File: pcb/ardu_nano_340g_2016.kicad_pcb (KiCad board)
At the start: 2 copper layers, 18.3 x 43.7 mm, 36 parts, among them J1 USB_B_Mini, J2 Conn_01x15, J3 Conn_01x15, J4 Conn_02x03_Odd_Even, U1 CH340G-JEC, U2 ATMEGA328P-AU, U3 LM1117-5.0, Y1 16MHz Resonator, Y2 12Mhz Resonator

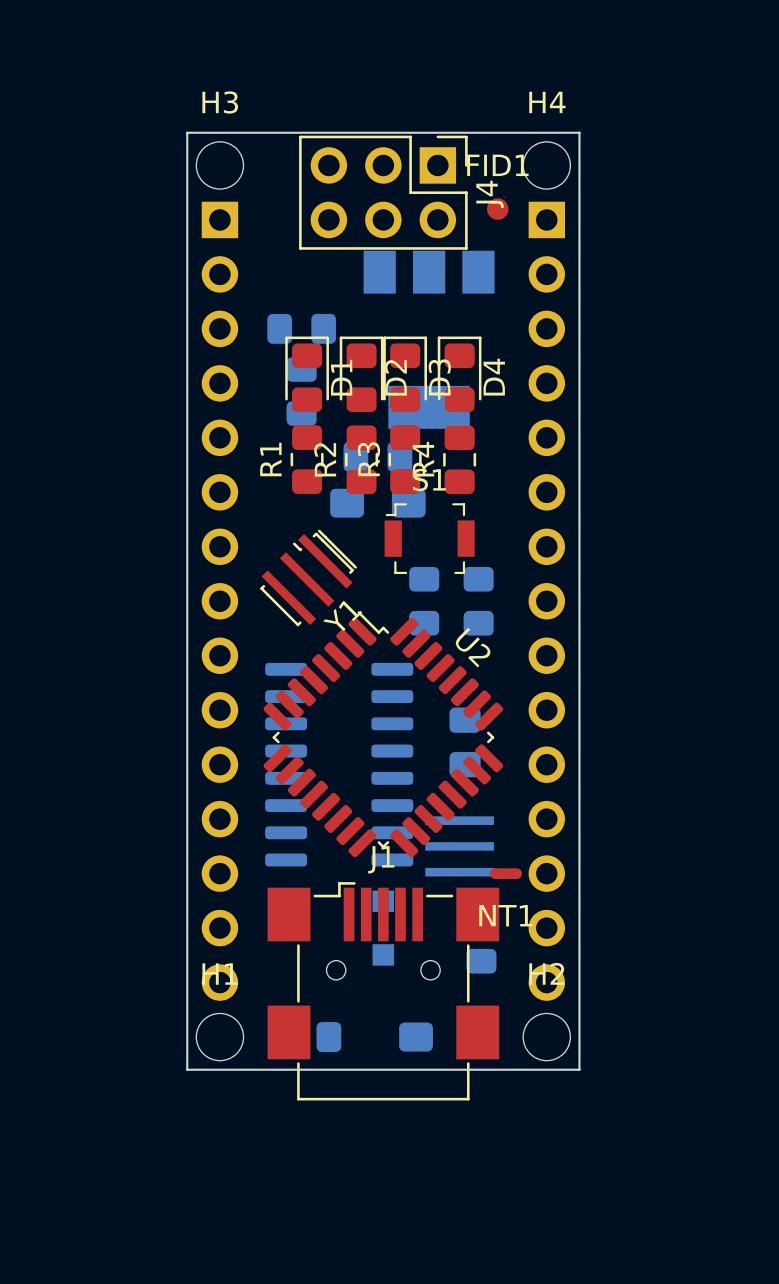
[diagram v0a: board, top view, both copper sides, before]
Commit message: V2.2 Se agregó capacitor desacople IC USB y se redujo huella resonadores
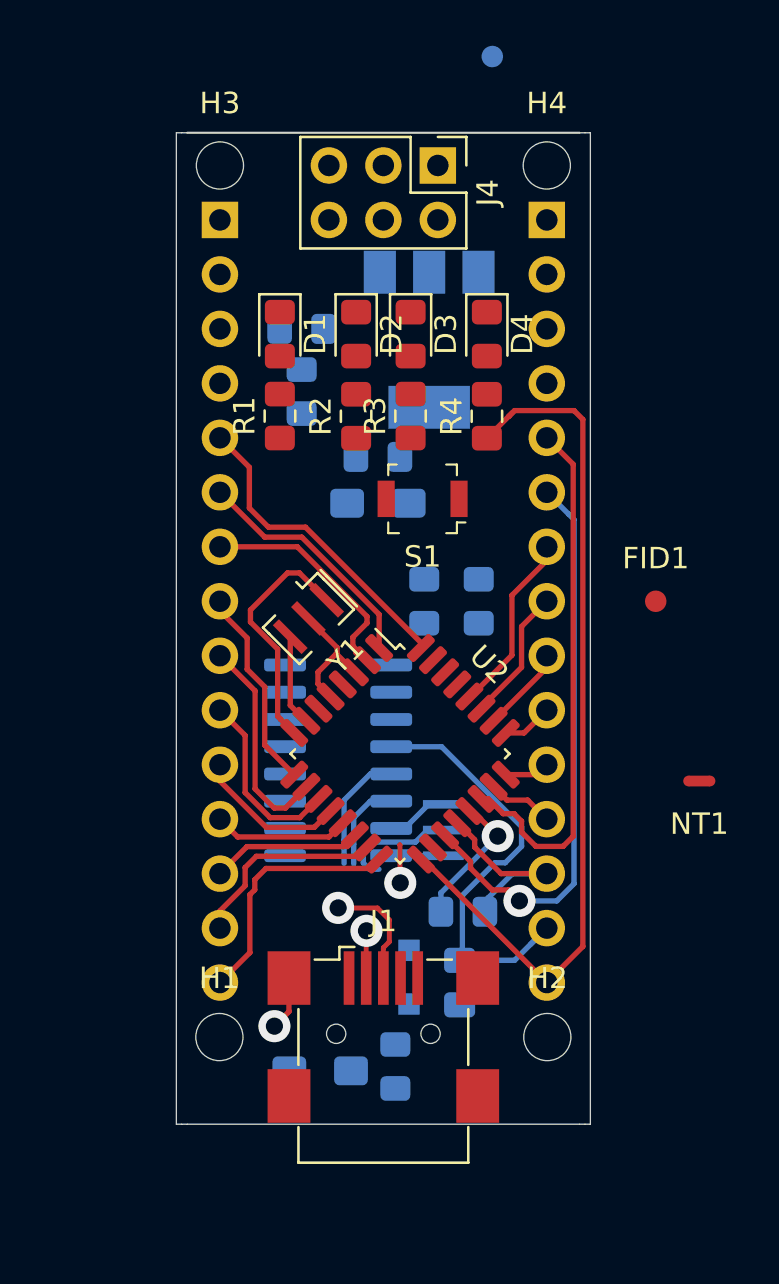
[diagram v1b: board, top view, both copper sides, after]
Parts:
- H1, H2: footprint MountingHole:MountingHole_2.2mm_M2_ISO14580 -> MountingHole:MountingHole_2.2mm_M2_ISO7380
- R1, R2, R3, R4, R5, R6: value R -> 1k
- R7: value R -> 10k
- Y1, Y2: footprint Crystal:Resonator_SMD_muRata_CSTxExxV-3Pin_3.0x1.1mm_HandSoldering -> Crystal:Resonator_SMD_muRata_CSTxExxV-3Pin_3.0x1.1mm
- moved FID2 41.7 mm to (134.6, 73.7)
- moved FID1 19.7 mm to (142.2, 99.1)
- moved C7 11.2 mm to (133.1, 116.8), turned to 270 degrees
- moved NT1 10.00 mm to (144.3, 107.4)
- moved C5 6.11 mm to (126.6, 121.0), turned to 180 degrees
- moved C4 4.35 mm to (130.1, 120.8), turned to 270 degrees
- moved J1 2.96 mm to (129.5, 119.2)
- moved D5 2.58 mm to (130.7, 116.6)
- moved D4 2.40 mm to (134.4, 86.6)
- moved R4 2.40 mm to (134.4, 90.4)
- moved D1 2.40 mm to (124.7, 86.6)
- moved R1 2.40 mm to (124.7, 90.4)
- moved D2 2.05 mm to (128.3, 86.6)
- moved D3 2.05 mm to (130.8, 86.6)
- moved R2 2.05 mm to (128.3, 90.4)
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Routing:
- net /D13_SCK: track 0.00 -> 40.6 mm
- net /A6: track 0.00 -> 28.1 mm, vias 0 -> 1
- net /A7: track 0.00 -> 24.8 mm
- net +3V3: track 0.00 -> 21.2 mm
- net /D2: track 0.00 -> 14.7 mm
- net GND: track 0.00 -> 14.2 mm, vias 0 -> 1
- net /D12_MISO: track 0.00 -> 11.7 mm
- net /D3: track 0.00 -> 11.5 mm
- net Net-(U2-Pad8): track 0.00 -> 11.4 mm
- net Net-(J1-Pad3): track 0.00 -> 11.1 mm, vias 0 -> 1
- net /D4: track 0.00 -> 10.8 mm
- net /AREF: track 0.00 -> 10.6 mm
- net /D5: track 0.00 -> 10.2 mm
- net /D6: track 0.00 -> 10.1 mm
- net /D11_MOSI: track 0.00 -> 9.38 mm
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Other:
- board size 18.3 x 43.7 mm -> 19.3 x 46.2 mm
- board text added: "TX RX PWR L"

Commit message: avances del 17/10/2020
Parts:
- added C8: 100nF, Capacitor_SMD:C_0805_2012Metric_Pad1.18x1.45mm_HandSolder, B.Cu at (127.4, 100.3)
- added C9: 100nF, Capacitor_SMD:C_0805_2012Metric_Pad1.18x1.45mm_HandSolder, F.Cu at (133.3, 113.9)
- NT1: moved to B.Cu
- Y1: value 16MHz Resonator -> 16MHz
- Y2: value 12Mhz Resonator -> 12Mhz
- moved NT1 13.6 mm to (132.7, 114.5), turned to 270 degrees
- moved C6 0.92 mm to (134.2, 113.7), turned to 270 degrees
- moved C7 0.47 mm to (133.5, 116.5), turned to 180 degrees
- moved D5 0.33 mm to (130.6, 116.9)
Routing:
- net +5V: track 0.00 -> 66.9 mm, vias 0 -> 1
- net GND: track 14.2 -> 73.1 mm, vias 1 -> 3
- net +3V3: track 21.2 -> 52.8 mm, vias 0 -> 2
- net VBUS: track 0.00 -> 12.8 mm, vias 0 -> 1
- net /D13_SCK: track 40.6 -> 49.1 mm
- net Net-(C1-Pad2): track 0.00 -> 6.30 mm
- net Net-(J1-Pad2): track 6.42 -> 12.0 mm
- net GNDA: track 6.50 -> 3.63 mm
- net (no net): track 1.79 -> 0.00 mm, vias 1 -> 0
- net Net-(J1-Pad3): track 11.1 -> 12.0 mm
- net /AREF: track 10.6 -> 9.75 mm

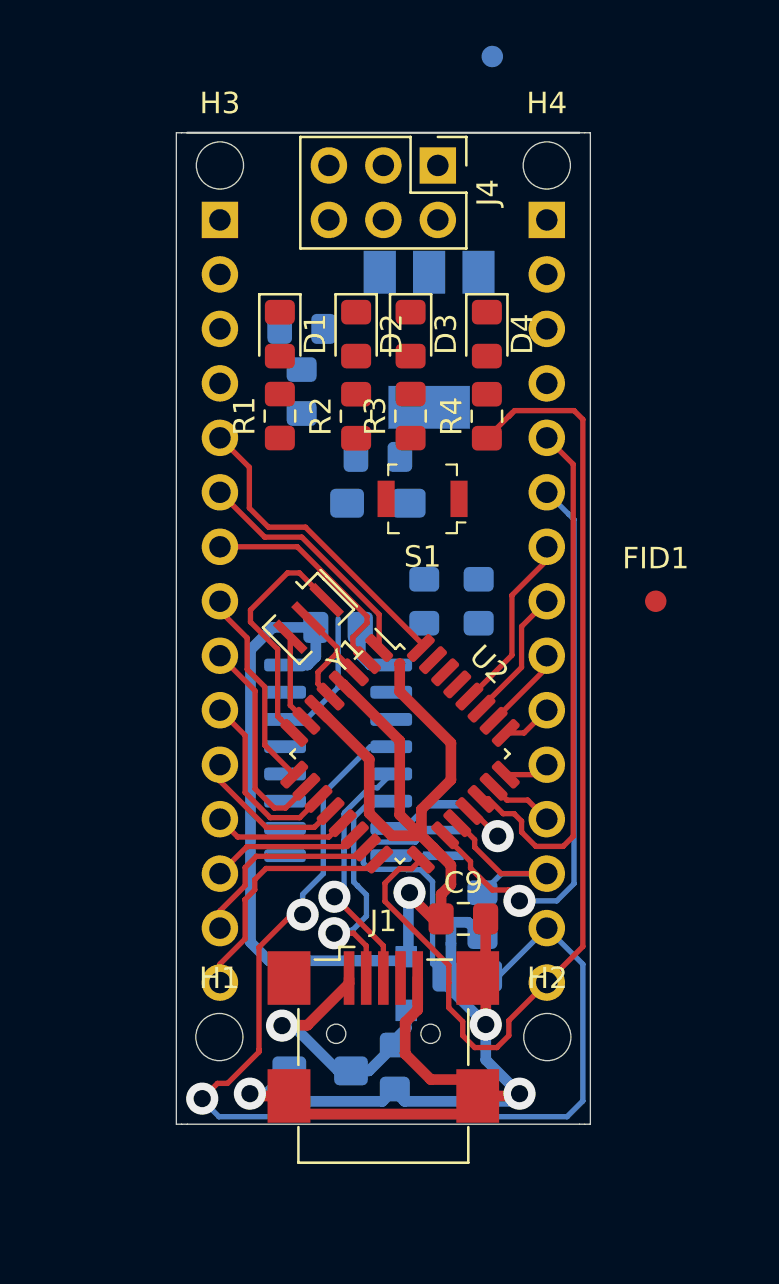
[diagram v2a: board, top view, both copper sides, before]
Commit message: ruteado completo
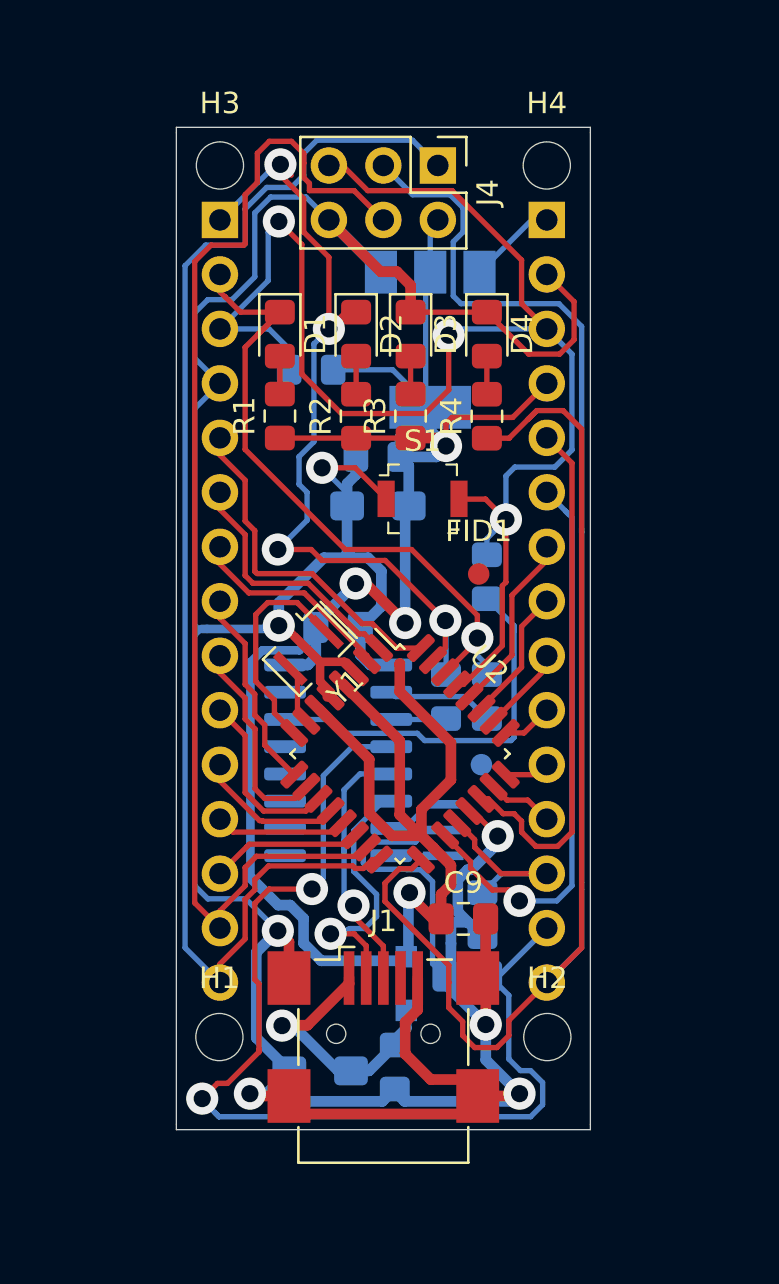
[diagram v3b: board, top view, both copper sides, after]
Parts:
- moved FID2 33.0 mm to (134.1, 106.7)
- moved C1 12.2 mm to (134.4, 97.9)
- moved FID1 8.35 mm to (134.0, 97.8)
- moved R5 5.32 mm to (134.4, 103.5)
- moved R6 4.70 mm to (132.5, 103.5)
- moved R7 1.96 mm to (126.2, 88.3)
- moved Y1 1.48 mm to (126.0, 101.3)
- moved C3 0.13 mm to (129.3, 94.6)
- moved U3 0.05 mm to (131.7, 86.9)
- turned S1 to 0 degrees
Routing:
- net GND: track 73.1 -> 177.1 mm, vias 3 -> 6
- net /RESET: track 0.00 -> 73.4 mm, vias 0 -> 3
- net /D12_MISO: track 11.7 -> 62.7 mm
- net +5V: track 66.9 -> 114.6 mm, vias 1 -> 4
- net /D11_MOSI: track 9.38 -> 57.1 mm
- net /D13_SCK: track 49.1 -> 95.8 mm
- net /TX1: track 0.00 -> 40.6 mm, vias 0 -> 4
- net /RX0: track 0.00 -> 33.5 mm, vias 0 -> 1
- net Net-(C1-Pad2): track 6.30 -> 18.3 mm
- net GNDA: track 3.63 -> 8.72 mm
- net Net-(R5-Pad2): track 0.00 -> 4.97 mm
- net +VDC: track 0.00 -> 4.15 mm
- net Net-(R6-Pad1): track 0.00 -> 2.57 mm
- net Net-(D4-Pad2): track 0.00 -> 1.78 mm
- net Net-(D2-Pad2): track 0.00 -> 1.78 mm
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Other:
- board size 19.3 x 46.2 mm -> 19.3 x 46.7 mm

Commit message: versión para fabricación casera con vias grandes
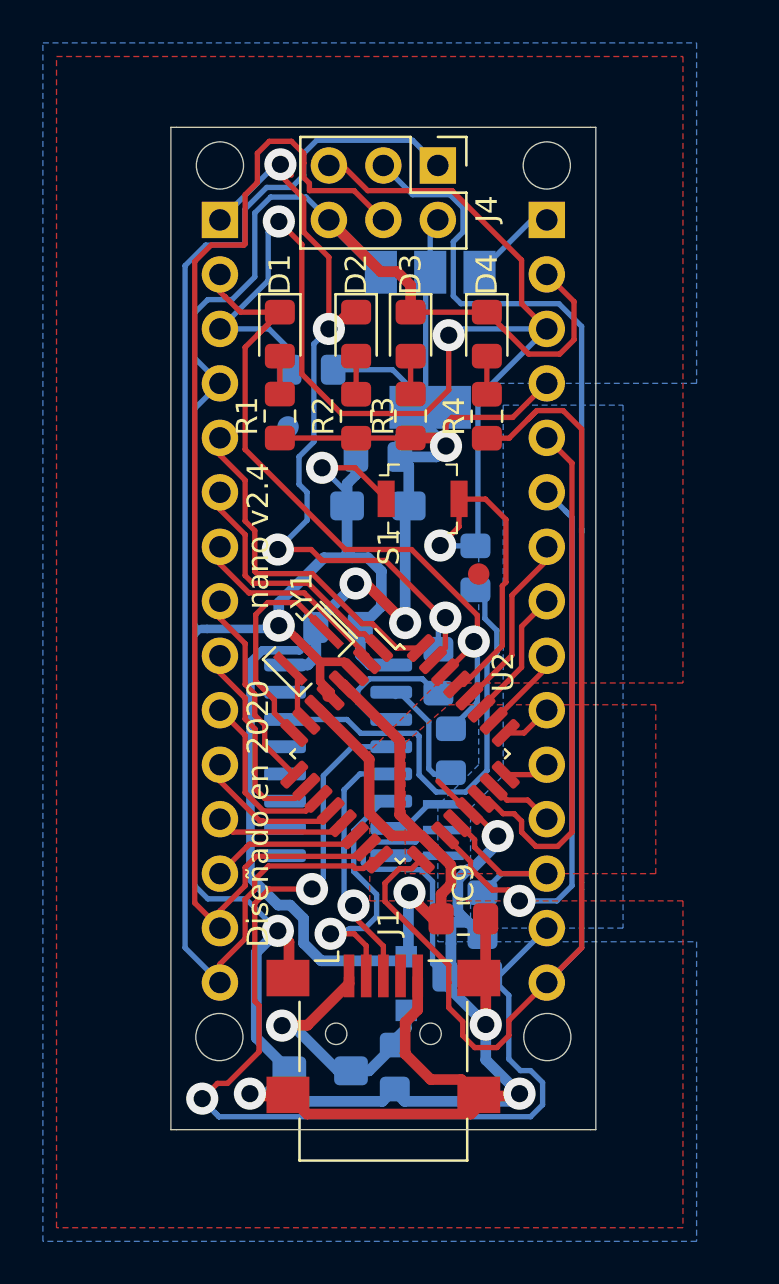
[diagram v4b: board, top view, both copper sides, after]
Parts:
- J1: footprint Connector_USB:USB_Mini-B_Wuerth_65100516121_Horizontal -> Connector_USB:USB_Mini-B_Lumberg_2486_01_Horizontal
- moved FID2 18.1 mm to (125.1, 90.9)
- moved R5 3.03 mm to (132.7, 106.0)
- moved R6 1.24 mm to (132.1, 102.3)
- moved C1 0.68 mm to (133.8, 97.5)
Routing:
- net +5V: track 114.6 -> 105.0 mm
- net Net-(R6-Pad1): track 2.57 -> 6.75 mm
- net Net-(C1-Pad2): track 18.3 -> 21.3 mm
- net /RESET: track 73.4 -> 76.1 mm
- net /RX0: track 33.5 -> 35.8 mm
- net GNDA: track 8.72 -> 10.8 mm
- net Net-(R5-Pad2): track 4.97 -> 5.87 mm
- net /TX1: track 40.6 -> 39.8 mm
- added copper zone on B.Cu, net GND
- added copper zone on F.Cu, net GND
- added copper zone on B.Cu, net GNDA
- added copper zone on F.Cu, net GNDA
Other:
- board size 19.3 x 46.7 mm -> 19.8 x 46.7 mm
- board text added: "Diseñado en 2020"
- board text added: "Minimos (Mayer 8 mils): Grillas 0,63mm, 0.254mm, 0.0508mm Pistas: 0.23mm, 0.25mm, 0.5mm Via: 1.5mm / 0.8mm Margen: 0.2mm Dist. a borde: 0.3mm Terminación: HASL"
- board text added: "nano v2.4"
